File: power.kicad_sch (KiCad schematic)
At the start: 6 parts, among them J4 10103592-0001LF, U2 AMS1117-3.3

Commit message: Update MCU schematic with VCAP capacitor. Draw boxes around communication busses and programming bus
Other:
- moved on the sheet: J4

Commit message: fix power supply scheme for microcontroller schematic
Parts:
- renumbered C7 to C11, C8 to C12, J4 to J1, R2 to R4
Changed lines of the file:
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@@
 		(in_pos_files yes)
 		(dnp no)
-		(property "Reference" "J4"
+		(property "Reference" "J1"
 			(at 115.57 62.23 0)
 			(show_name no)
@@
 			(project "SmallFlightV1"
 				(path "/5a8b04a1-a6d6-48bd-ac5f-d4986cb92d03/e79f4bae-0570-408a-a4f8-ca387aa7c020"
-					(reference "J4")
+					(reference "J1")
 					(unit 1)
 				)
@@
 		(dnp no)
 		(fields_autoplaced yes)
-		(property "Reference" "#PWR04"
+		(property "Reference" "#PWR08"
 			(at 119.38 91.44 0)
 			(hide yes)
@@
 			(project "SmallFlightV1"
 				(path "/5a8b04a1-a6d6-48bd-ac5f-d4986cb92d03/e79f4bae-0570-408a-a4f8-ca387aa7c020"
-					(reference "#PWR04")
+					(reference "#PWR08")
 					(unit 1)
 				)
@@
 		(dnp no)
 		(fields_autoplaced yes)
-		(property "Reference" "C8"
+		(property "Reference" "C12"
 			(at 182.88 74.2949 0)
 			(show_name no)
@@
 			(project "SmallFlightV1"
 				(path "/5a8b04a1-a6d6-48bd-ac5f-d4986cb92d03/e79f4bae-0570-408a-a4f8-ca387aa7c020"
-					(reference "C8")
+					(reference "C12")
 					(unit 1)
 				)
@@
 		(dnp no)
 		(fields_autoplaced yes)
-		(property "Reference" "#PWR07"
+		(property "Reference" "#PWR09"
 			(at 154.94 92.71 0)
 			(hide yes)
@@
 			(project "SmallFlightV1"
 				(path "/5a8b04a1-a6d6-48bd-ac5f-d4986cb92d03/e79f4bae-0570-408a-a4f8-ca387aa7c020"
-					(reference "#PWR07")
+					(reference "#PWR09")
 					(unit 1)
 				)
@@
 		(in_pos_files yes)
 		(dnp no)
-		(property "Reference" "R2"
+		(property "Reference" "R4"
 			(at 193.294 69.85 0)
 			(show_name no)
@@
 			(project "SmallFlightV1"
 				(path "/5a8b04a1-a6d6-48bd-ac5f-d4986cb92d03/e79f4bae-0570-408a-a4f8-ca387aa7c020"
-					(reference "R2")
+					(reference "R4")
 					(unit 1)
 				)
@@
 		(dnp no)
 		(fields_autoplaced yes)
-		(property "Reference" "C7"
+		(property "Reference" "C11"
 			(at 158.75 73.6599 0)
 			(show_name no)
@@
 			(project "SmallFlightV1"
 				(path "/5a8b04a1-a6d6-48bd-ac5f-d4986cb92d03/e79f4bae-0570-408a-a4f8-ca387aa7c020"
-					(reference "C7")
+					(reference "C11")
 					(unit 1)
 				)

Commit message: remove redundant stm32f44 document folder. remove USB pinouts and references
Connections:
- net USB_DN: no longer names the net of J1.2 (D-)
- net USB_DP: no longer names the net of J1.3 (D+)
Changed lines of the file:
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@@
-	(wire
-		(pts
-			(xy 116.84 68.58) (xy 129.54 68.58)
-		)
-		(stroke
-			(width 0)
-			(type default)
-		)
-	)
 	(wire
 		(pts
@@
 	(wire
 		(pts
-			(xy 116.84 71.12) (xy 129.54 71.12)
-		)
-		(stroke
-			(width 0)
-			(type default)
-		)
-	)
-	(wire
-		(pts
 			(xy 154.94 83.82) (xy 168.91 83.82)
 		)
@@
 		)
 	)
-	(hierarchical_label "USB_DN"
-		(shape input)
-		(at 129.54 68.58 0)
-		(effects
-			(font
-				(size 1.27 1.27)
-			)
-			(justify left)
-		)
-	)
-	(hierarchical_label "USB_DP"
-		(shape input)
-		(at 129.54 71.12 0)
-		(effects
-			(font
-				(size 1.27 1.27)
-			)
-			(justify left)
-		)
-	)

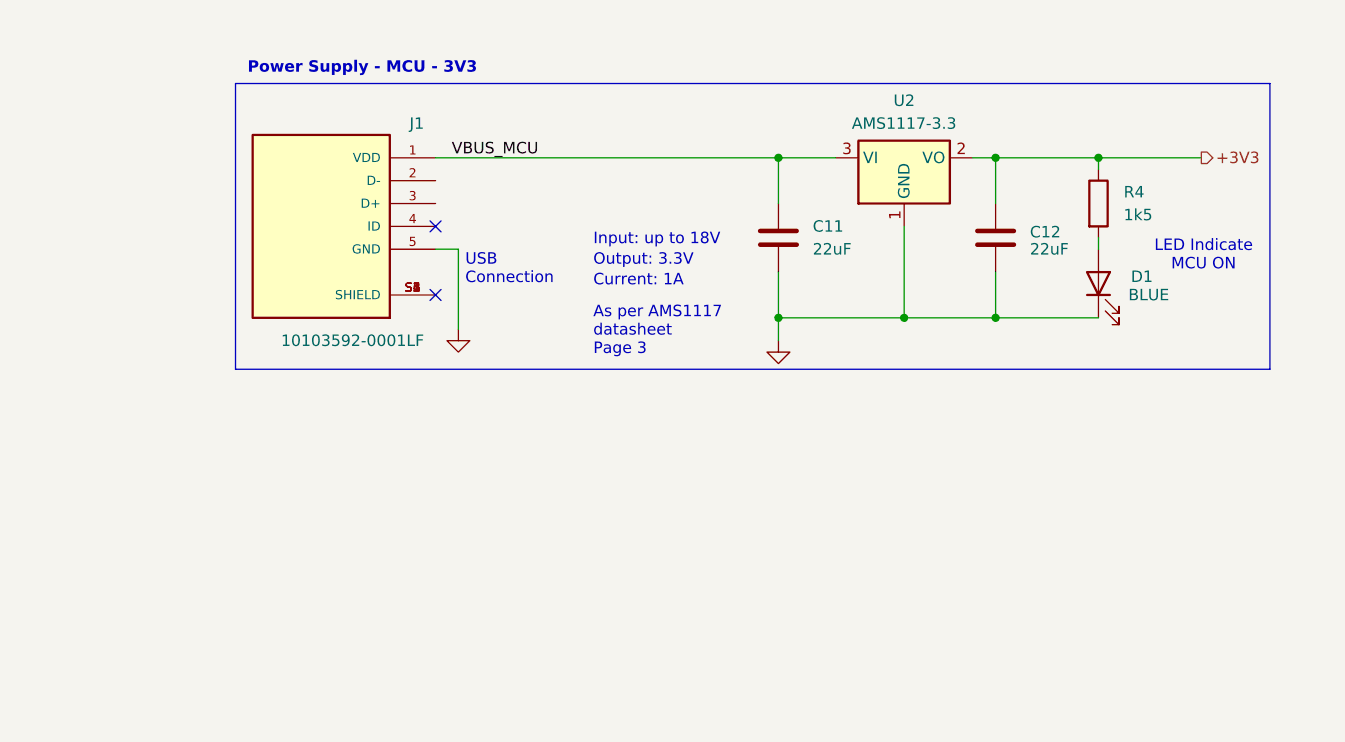
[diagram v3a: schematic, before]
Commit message: replace usb interface with usb-c. add data lines for it too
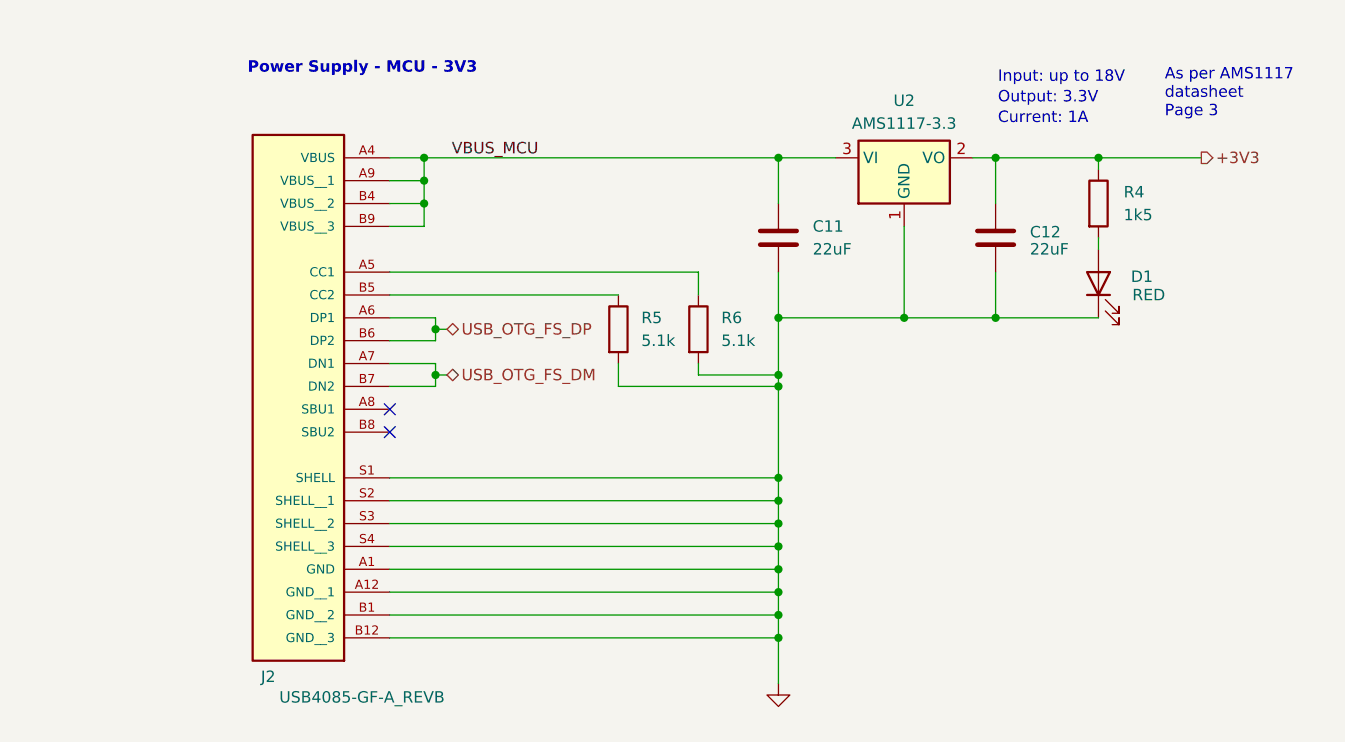
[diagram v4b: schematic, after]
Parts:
- removed J1: 10103592-0001LF, 10103592-0001LF:AMPHENOL_10103592-0001LF, symbol USB conn:10103592-0001LF
- added J2: USB4085-GF-A_REVB, USB4085-GF-A_REVB:GCT_USB4085-GF-A_REVB, symbol USB4085-GF-A_REVB:USB4085-GF-A_REVB
- added R5, R6: 5.1k, symbol Device:R
- D1: value BLUE -> RED
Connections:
- net GND: now also J2.A1 (GND), J2.A12 (GND__1), J2.B1 (GND__2), J2.B12 (GND__3), J2.S1 (SHELL), J2.S2 (SHELL__1), J2.S3 (SHELL__2), J2.S4 (SHELL__3), R5.2, R6.2
- net VBUS_MCU: now also J2.A4 (VBUS), J2.A9 (VBUS__1), J2.B4 (VBUS__2), J2.B9 (VBUS__3)
- new net: J2.A5 (CC1), R6.1
- new net: J2.B5 (CC2), R5.1
- new net USB_OTG_FS_DM: J2.A7 (DN1), J2.B7 (DN2)
- new net USB_OTG_FS_DP: J2.A6 (DP1), J2.B6 (DP2)
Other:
- note removed: "LED Indicate MCU ON"
- note removed: "USB Connection"

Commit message: wiring the IMU as per its datasheet app circuit. started with power rails
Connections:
- net VBUS_MCU: no longer names the net of C11.1, J2.A4 (VBUS), J2.A9 (VBUS__1), J2.B4 (VBUS__2), J2.B9 (VBUS__3), U2.3 (VI)
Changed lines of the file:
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@@
-		)
-	)
-	(label "VBUS_MCU"
-		(at 128.27 66.04 180)
-		(effects
-			(font
-				(size 1.27 1.27)
-			)
-			(justify right bottom)
 		)
 	)

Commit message: update README. update imu to select address, add notte
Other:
- note added: "USB-C Power Supply"
- note removed: "Power Supply - MCU - 3V3"
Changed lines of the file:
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@@
 	(generator_version "10.0")
 	(paper "A4")
+	(rectangle
+		(start 88.265 53.34)
+		(end 215.265 128.905)
+		(stroke
+			(width 0)
+			(type default)
+		)
+		(fill
+			(type none)
+		)
+	)
 	(text "Current: 1A"
 		(exclude_from_sim no)
@@
 		)
 	)
-	(text "Power Supply - MCU - 3V3"
+	(text "USB-C Power Supply"
 		(exclude_from_sim no)
-		(at 108.712 56.134 0)
+		(at 99.06 52.07 0)
 		(effects
 			(font
